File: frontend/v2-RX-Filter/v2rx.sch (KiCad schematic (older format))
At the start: 64 parts, among them P1 CONN_01X09, P4 CONN_01X02, P5 CONN_01X02, U1 4504, U10 PE4259-53, U11 PE4259-53, U12 PE4259-53, U2 PE4259-53, U3 PE4259-53, U4 PE4259-53, U5 PE4259-53, U6 PE4259-53, U7 PE4259-53, U8 PE4259-53, U9 PE4259-53

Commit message: new kicad 4.0.1 stable
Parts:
- C1, C10, C11, C12, C13, C14, C15, C16, C17, C18, C19, C2, C20, C21, C22, C23, C24, C25, C26, C3, C4, C5, C6, C7, C8, C9: symbol C -> C-RESCUE-v2rx
- P1: footprint (none) -> Socket_Strips:Socket_Strip_Straight_1x09
- U1: footprint (none) -> Housings_SOIC:SOIC-16_3.9x9.9mm_Pitch1.27mm
- U10, U11, U12, U2, U3, U4, U5, U6, U7, U8, U9: footprint (none) -> HERMESLITE:sc70-6

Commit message: v2rx changes and update to new kicad
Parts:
- removed C7: 150pF, HERMESLITE:C_0805, symbol C-RESCUE-v2rx
- removed L20: 270nH, HERMESLITE:Choke_SMD_1206_Standard, symbol INDUCTOR
- removed L22: 680nH, HERMESLITE:Choke_SMD_1206_Standard, symbol INDUCTOR
- removed L23: 1.5uH, HERMESLITE:Choke_SMD_1206_Standard, symbol INDUCTOR
- removed P1: CONN_01X09, Socket_Strips:Socket_Strip_Straight_1x09, symbol CONN_01X09
- removed U7: PE4259-53, HERMESLITE:sc70-6, symbol PE4259-53
- added C1, C52, C74, C80, C81: 0.1uF, HERMESLITE:C_0805, symbol C-RESCUE-v2rx
- added C17, C30, C31, C32, C33, C34, C35, C36, C38, C46, C53, C54, C55, C56, C57, C58, C59, C6, C61, C67, C68, C69, C70, C71, C73: DNI, HERMESLITE:C_0805, symbol C-RESCUE-v2rx
- added C26, C48, C64: 330pF, HERMESLITE:C_0805, symbol C-RESCUE-v2rx
- added C27, C49, C65: 560pF, HERMESLITE:C_0805, symbol C-RESCUE-v2rx
- added C29, C43, C51: 1500pF, HERMESLITE:C_0805, symbol C-RESCUE-v2rx
- added C37, C45, C62: 120pF, HERMESLITE:C_0805, symbol C-RESCUE-v2rx
- added C39, C40: 270pF, HERMESLITE:C_0805, symbol C-RESCUE-v2rx
- added C41: 680pF, HERMESLITE:C_0805, symbol C-RESCUE-v2rx
- added C44, C75, C76, C77, C78, C79, C82: 0.01uF, HERMESLITE:C_0805, symbol C-RESCUE-v2rx
- added C47, C63: 180pF, HERMESLITE:C_0805, symbol C-RESCUE-v2rx
- added C50: 1200pF, HERMESLITE:C_0805, symbol C-RESCUE-v2rx
- added C60: 68pF, HERMESLITE:C_0805, symbol C-RESCUE-v2rx
- added C66: 1000pF, HERMESLITE:C_0805, symbol C-RESCUE-v2rx
- added FB1, FB2: BLM21PG220SN1D, symbol FILTER
- added L19: 2.2uH, HERMESLITE:Choke_SMD_1206_Standard, symbol INDUCTOR
- added P1: CONN_02X07, symbol CONN_02X07
- added P3, P4: CONN_02X03, symbol CONN_02X03
- added U10, U11, U2, U3: PE4259-53, HERMESLITE:sc70-6, symbol PE4259-53
- added U9: 4504, Housings_SOIC:SOIC-16_3.9x9.9mm_Pitch1.27mm, symbol 4504
- C10, C11, C12: value 150pF -> DNI
- C13: value 390pF -> DNI
- C14: value 680pF -> DNI
- C15: value 1200pF -> DNI
- C16: value 1000pF -> 68pF
- C18: value 39pF -> 120pF
- C19: value 56pF -> 180pF
- C2: value 100pF -> DNI
- C20: value 150pF -> 330pF
- C21: renamed from C6; value 150pF -> 560pF
- C22: value 150pF -> 1000pF
- C23: value 150pF -> 120pF
- C24, C3: value 270pF -> DNI
- C25: value 560pF -> 180pF
- C28: renamed from C17; value 2200pF -> 1200pF
- C4: value 560pF -> DNI
- C42: renamed from C21; value 150pF -> 1200pF
- C5: value 1000pF -> DNI
- C7: renamed from C1; value 1000pF -> DNI
- C72: renamed from C26; value 1000pF -> DNI
- C8: value 39pF -> DNI
- C9: value 56pF -> DNI
- L1: value 270nH -> 680nH
- L10: value 4.7uH -> 820nH
- L11: value 100nH -> 1.5uH
- L12: value 150nH -> 2.2uH
- L13: value 330nH -> 3.9uH
- L14: value 680nH -> 8.2uH
- L15: value 1.5uH -> 680nH
- L16: value 1uH -> DNI
- L17: value 1.8uH -> 820nH
- L18: value 2.7uH -> 1.5uH
- L2: value 390nH -> DNI
- L20: renamed from L19; value 4.7uH -> 3.9uH
- L21: value 390nH -> 8.2uH
- L3: value 680nH -> 820nH
- L5: value 1.5uH -> 2.2uH
- L6: value 4.7uH -> 3.9uH
- L7: value 1uH -> 8.2uH
- L8: value 1.8uH -> 680nH
- L9: value 2.7uH -> DNI
- renumbered P4 to P2, U8 to U12, U9 to U13, U10 to U14, U11 to U15, U12 to U16, U2 to U4, U3 to U5, U4 to U6, U5 to U7, U6 to U8
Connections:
- net GND: now also C8.2, U12.1 (RF1), U13.1 (RF1), U14.1 (RF1), U15.1 (RF1), U4.1 (RF1), U5.1 (RF1), U6.1 (RF1), U7.1 (RF1), C26.2, C27.2, C29.2, C44.1, C45.2, C46.2, C47.2, C48.2, C49.2, C50.2, C51.2, C52.2, C6.2, C67.2, C68.2, C69.2, C70.2, C71.2, C73.2, C75.1, C76.1, C77.1, C78.1, C79.1, C80.2, C81.1, C82.1, P1.2 (P2), P1.4 (P4), P1.6 (P6), P3.2 (P2), P3.4 (P4), P3.6 (P6), P4.2 (P2), P4.4 (P4), P4.6 (P6), U10.2 (GND), U11.1 (RF1), U11.2 (GND), U2.2 (GND), U3.1 (RF1), U3.2 (GND), U9.8 (VSS); no longer C13.2, C14.2, C15.2, C16.2, L1.2, L11.2, L12.2, L13.2, L14.2, L15.2, L2.2, L21.2, L3.2, L4.2, L5.2, U12.3 (RF2), U13.3 (RF2), U14.3 (RF2), U15.3 (RF2), U4.3 (RF2), U5.3 (RF2), U6.3 (RF2), U7.3 (RF2)
- net at C2.1, L1.1: now also C9.2, U2.5 (RFC); no longer L7.1, U4.5 (RFC)
- net at L7.2: now also C15.1, C22.2; no longer C8.2
- net at C18.2: now also C11.1, L3.2; no longer L16.2
- net at C4.1, L3.1: now also C11.2, U4.5 (RFC); no longer L9.1, U6.5 (RFC)
- net at C10.2: now also C3.1, L2.1, U3.5 (RFC); no longer L9.2
- net at C20.2: now also C13.1, L5.2; no longer L18.2
- net at L8.2: now also C30.1, C37.2; no longer C9.2
- net at C19.2: now also C12.1, L4.2; no longer L17.2
- net at C7.1, L6.1, U7.5 (RFC): now also C14.2; no longer L4.1
- net at C21.1, C28.1: now also L13.1, C35.2; no longer L14.1, L20.1
- net at C21.2, L6.2: now also C14.1
- net at C72.1, U15.5 (RFC): now also C65.1; no longer C22.1, C42.1
- net at U1.14 (Fin): now also P1.1 (P1)
- net at U1.9 (Din): now also P1.5 (P5)
- net at U1.11 (Ein): now also P1.7 (P7)
- net at U1.7 (Cin): now also P1.9 (P9)
- net at U1.5 (Bin): now also P1.11 (P11)
- net at U1.3 (Ain): now also P1.12 (P12)
- net at U1.15 (Fout): now also U10.4 (CTRL), U2.4 (CTRL)
- net 3.3V: no longer names the net of U1.16 (VDD), U12.6 (/CTRL), U13.6 (/CTRL), U14.6 (/CTRL), U15.6 (/CTRL), U16.6 (/CTRL), U4.6 (/CTRL), U5.6 (/CTRL), U6.6 (/CTRL), U7.6 (/CTRL), U8.6 (/CTRL)
- net 3.3V: now also C81.2, FB2.2, U10.6 (/CTRL), U11.6 (/CTRL), U2.6 (/CTRL), U3.6 (/CTRL), U9.16 (VDD)
- net 5V: no longer names the net of U1.1 (VCC), U1.13 (Select)
- net 5V: now also C52.1, C80.1, FB1.2, U9.1 (VCC), U9.13 (Select)
- new net: C74.1, P5.2 (P2)
- new net: C1.2, P2.2 (P2)
- new net: C42.1, C50.1, C58.2, L20.1
- new net: C35.1, C42.2, L13.2
- new net: C58.1, C65.2, L20.2
- new net: C1.1, P3.3 (P3), U3.3 (RF2), U4.3 (RF2), U5.3 (RF2), U6.3 (RF2), U7.3 (RF2), U8.3 (RF2)
- new net: C15.2, C8.1, L7.1, U8.5 (RFC)
- new net: C74.2, P4.3 (P3), U11.3 (RF2), U12.3 (RF2), U13.3 (RF2), U14.3 (RF2), U15.3 (RF2), U16.3 (RF2)
- new net: C66.1, C73.1, U16.5 (RFC)
- new net: C13.2, C6.1, L5.1, U6.5 (RFC)
- new net: C12.2, C5.1, L4.1, U5.5 (RFC)
- new net: C64.1, C71.1, U14.5 (RFC)
- new net: C63.1, C70.1, U13.5 (RFC)
- new net: C62.1, C69.1, U12.5 (RFC)
- new net: FB1.1, P1.10 (P10)
- new net: FB2.1, P1.13 (P13)
- new net: P1.3 (P3), U9.3 (Ain)
- new net: C22.1, C29.1, C36.2, L14.1
- new net: C43.1, C51.1, C59.2, L21.1
- new net: C36.1, C43.2, L14.2
- new net: C59.1, C66.2, L21.2
- new net: C20.1, C27.1, C34.2, L12.1
- new net: C41.1, C49.1, C57.2, L19.1
- new net: C34.1, C41.2, L12.2
- new net: C57.1, C64.2, L19.2
- new net: C19.1, C26.1, C33.2, L11.1
- new net: C40.1, C48.1, C56.2, L18.1
- new net: C33.1, C40.2, L11.2
- new net: C56.1, C63.2, L18.2
- new net: C18.1, C25.1, C32.2, L10.1
- new net: C39.1, C47.1, C55.2, L17.1
- new net: C32.1, C39.2, L10.2
- new net: C55.1, C62.2, L17.2
- new net: U11.4 (CTRL), U3.4 (CTRL), U9.2 (Aout)
- new net: C61.1, C68.1, U11.5 (RFC)
- new net: C17.1, C24.1, C31.2, L9.1
- new net: C10.1, C17.2, L2.2
- new net: C38.1, C46.1, C54.2, L16.1
- new net: C31.1, C38.2, L9.2
- new net: C54.1, C61.2, L16.2
- new net: P3.1 (P1), U2.1 (RF1)
- new net: P3.5 (P5), U2.3 (RF2)
- new net: P4.1 (P1), U10.1 (RF1)
- new net: P4.5 (P5), U10.3 (RF2)
- new net: C60.1, C67.1, U10.5 (RFC)
- new net: C16.1, C23.1, C30.2, L8.1
- new net: C16.2, C9.1, L1.2
- new net: C37.1, C45.1, C53.2, L15.1
- new net: C53.1, C60.2, L15.2
- no-connect marks 2 -> 13
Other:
- note added: "(DNI)"
- note added: "10/12M\n"
- note added: "160M\n"
- note added: "17/15M\n"
- note added: "30/20M\n"
- note added: "3v3 from\nV2 frontend"
- note added: "60/40M\n"
- note added: "80/75M\n"
- note added: "Common brings in\n 12V from PA"
- note added: "From pre-V2 TX design\nBand0 - 160M\nBand1 - 80/75M\nBand2 - 60/40M\nBand3 - 30/20M\nBand4 - 17/15M\nBand5 - spare\nBand6 - 10/12M inverted"
- note added: "Jumper Pins 3 to 5 if normal logic\nJumper pins 1 - 3 if inverted logic\nGround unused pin to 2, 4 or 6 as needed"
- note added: "Spare\n"
- note removed: "14-20MHz values,\nneeds 30M/20M BPF"
- note removed: "160M"
- note removed: "20-30MHz values,\nneeds to be 17m/15m BPF"
- note removed: "3-5MHz\nMay want to tighten this up to 4mhz"
- note removed: "7-10MHz values,\nneeds to be 60M/40M BPF"
- note removed: "Band0\nBand1\nBand2\nBand3\nBand4\nBand5\nBand6\nextra\nGnd"
- note removed: "Bypass"
- note removed: "From pre-V2 TX design\nBand0 - 160M\nBand1 - 80/75M\nBand2 - 60/40M\nBand3 - 30/20M\nBand4 - 17/15M\nBand5 - unused\nBand6 - 10/12M inverted"
- note removed: "Notes - Need to determine how to obtain\n3.3V and 5V - 12v with regulators on board or\njumper from v2 main board to supply voltages."
- moved on the sheet: C21, C28, C42, C7, C72, L20, L6, P2, P5, U1, U12, U13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

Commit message: Latest Rx updates
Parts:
- FB1, FB2: footprint (none) -> Resistors_SMD:R_0805_HandSoldering
- L1, L10, L11, L12, L13, L14, L15, L16, L17, L18, L19, L2, L20, L21, L3, L4, L5, L6, L7, L8, L9: footprint HERMESLITE:Choke_SMD_1206_Standard -> HERMESLITE:inductor
- P1: footprint (none) -> Pin_Headers:Pin_Header_Straight_2x07
- P3, P4: footprint (none) -> Pin_Headers:Pin_Header_Straight_2x03
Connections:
- net at U1.2 (Aout), U16.4 (CTRL), U8.4 (CTRL): now also C82.2
- net at U1.4 (Bout), U15.4 (CTRL), U7.4 (CTRL): now also C79.2
- net at U1.6 (Cout), U14.4 (CTRL), U6.4 (CTRL): now also C78.2
- net at U1.10 (Dout), U13.4 (CTRL), U5.4 (CTRL): now also C77.2
- net at U1.12 (Eout), U12.4 (CTRL), U4.4 (CTRL): now also C76.2
- net at U1.15 (Fout), U10.4 (CTRL), U2.4 (CTRL): now also C44.2
- net at U11.4 (CTRL), U3.4 (CTRL), U9.2 (Aout): now also C75.2

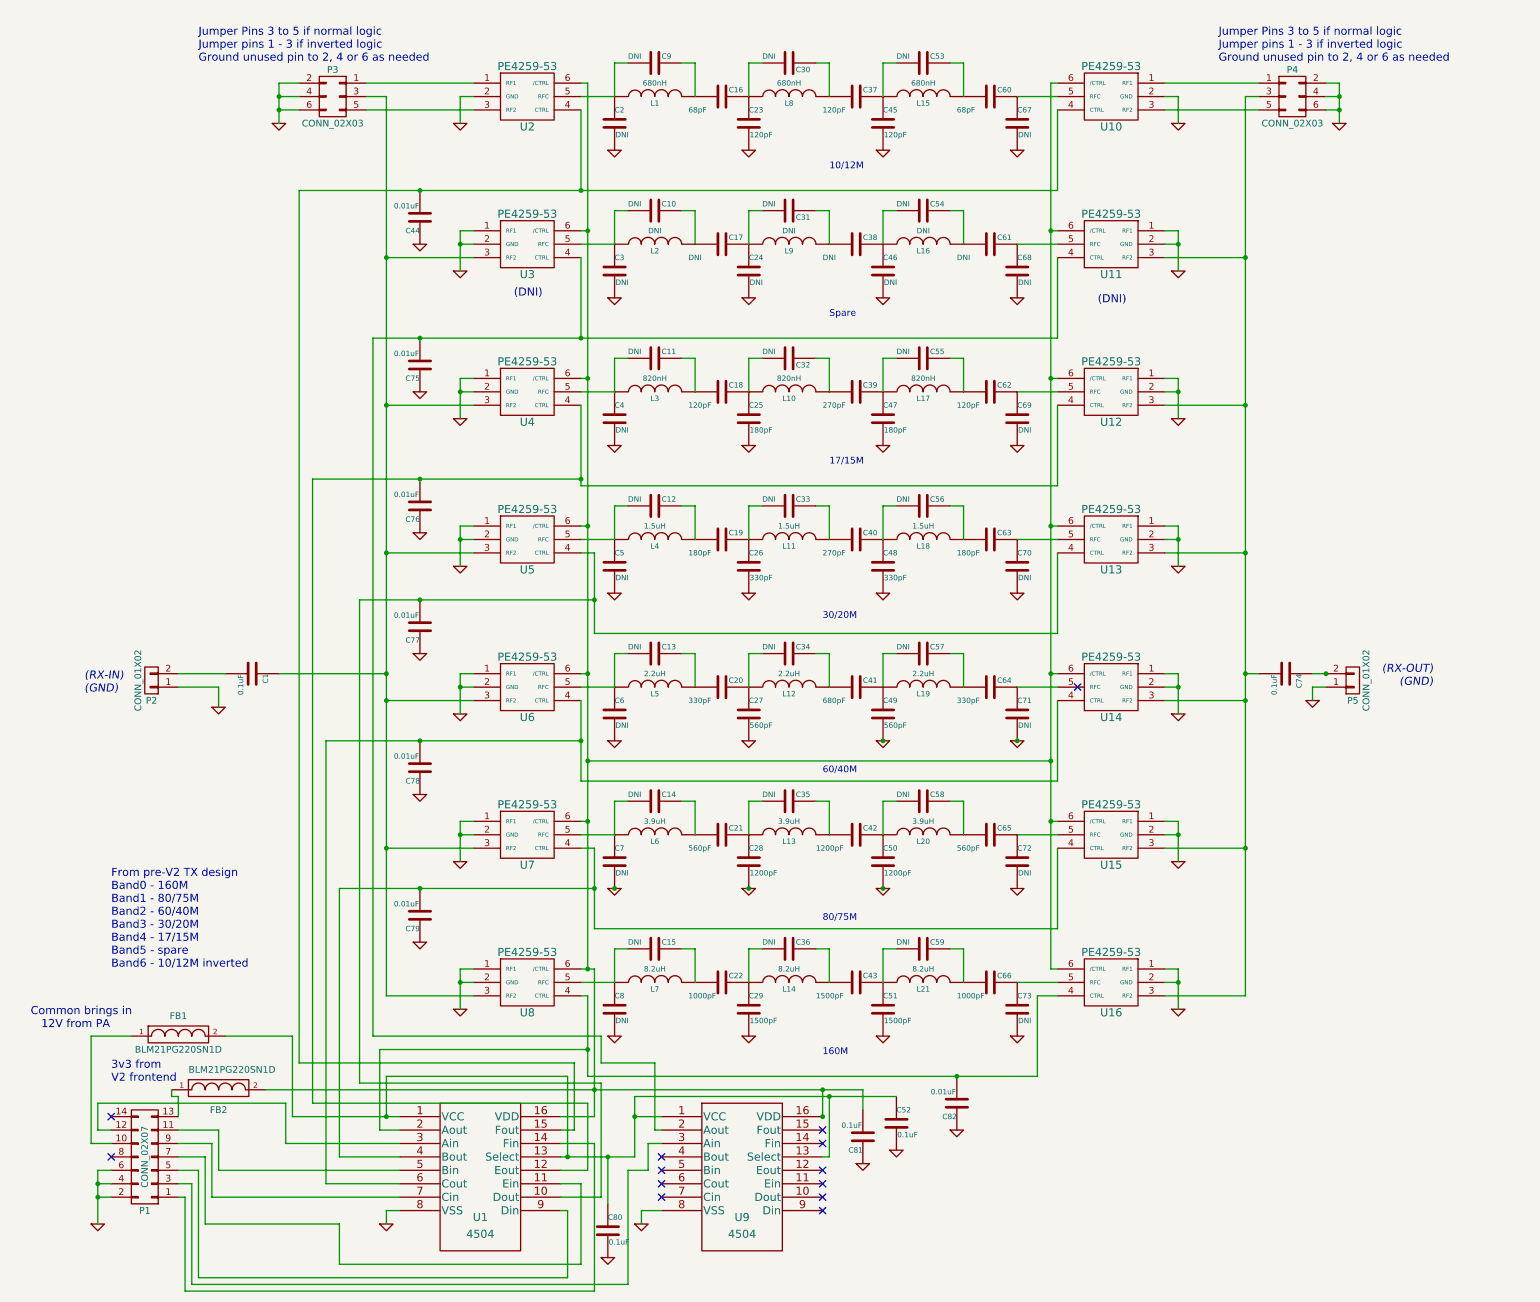
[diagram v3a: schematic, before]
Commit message: New RX Filter Board Layout
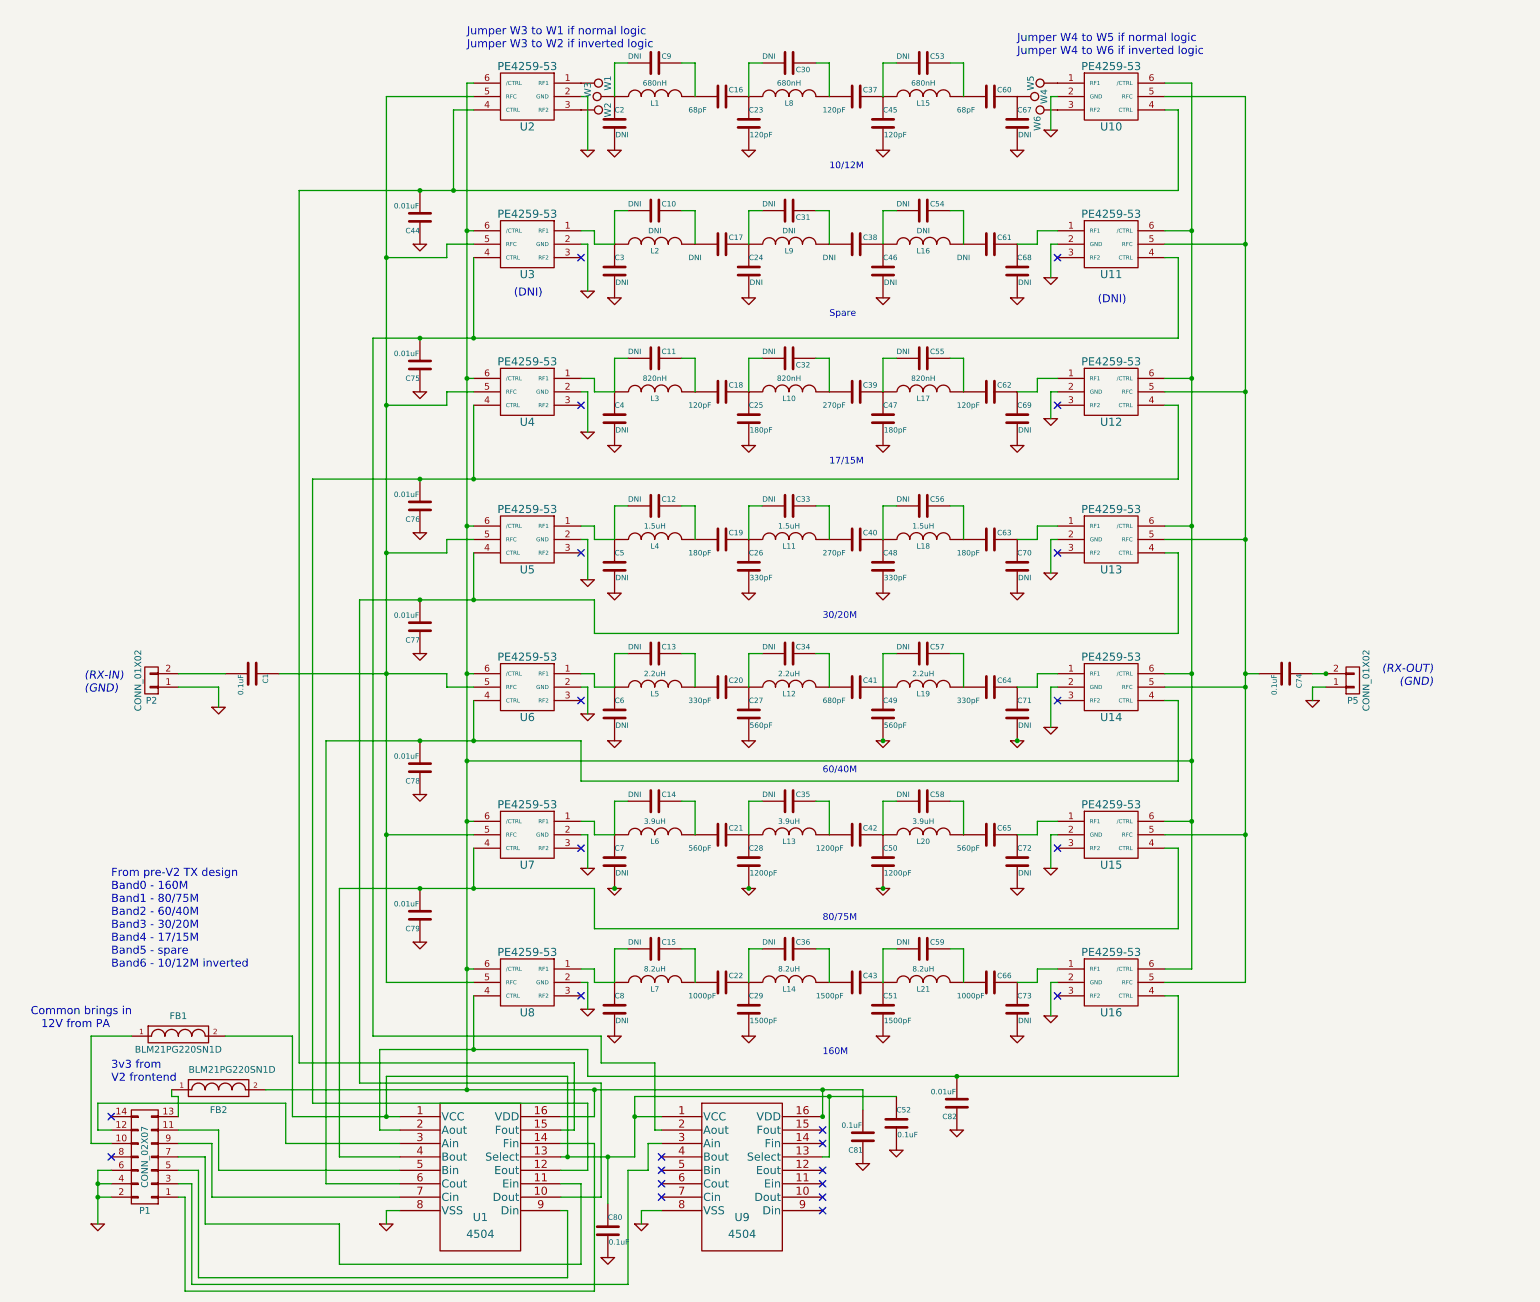
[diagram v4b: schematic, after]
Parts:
- removed P3, P4: CONN_02X03, Pin_Headers:Pin_Header_Straight_2x03, symbol CONN_02X03
- added W1, W2, W3, W4, W5, W6: TEST_1P, Wire_Pads:SolderWirePad_single_0-8mmDrill, symbol TEST_1P
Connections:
- net GND: no longer U11.1 (RF1), U12.1 (RF1), U13.1 (RF1), U14.1 (RF1), U15.1 (RF1), U16.1 (RF1), U3.1 (RF1), U4.1 (RF1), U5.1 (RF1), U6.1 (RF1), U7.1 (RF1), U8.1 (RF1)
- net at C14.2, C7.1, L6.1: now also U7.1 (RF1); no longer U7.5 (RFC)
- net at C65.1, C72.1: now also U15.1 (RF1); no longer U15.5 (RFC)
- net at C15.2, C8.1, L7.1: now also U8.1 (RF1); no longer U8.5 (RFC)
- net at C66.1, C73.1: now also U16.1 (RF1); no longer U16.5 (RFC)
- net at C13.2, C6.1, L5.1: now also U6.1 (RF1); no longer U6.5 (RFC)
- net at C12.2, C5.1, L4.1: now also U5.1 (RF1); no longer U5.5 (RFC)
- net at C11.2, C4.1, L3.1: now also U4.1 (RF1); no longer U4.5 (RFC)
- net at C64.1, C71.1: now also U14.1 (RF1); no longer U14.5 (RFC)
- net at C63.1, C70.1: now also U13.1 (RF1); no longer U13.5 (RFC)
- net at C62.1, C69.1: now also U12.1 (RF1); no longer U12.5 (RFC)
- net at C10.2, C3.1, L2.1: now also U3.1 (RF1); no longer U3.5 (RFC)
- net at C61.1, C68.1: now also U11.1 (RF1); no longer U11.5 (RFC)
- net at U2.1 (RF1): now also W1.1
- net at U2.3 (RF2): now also W2.1
- net at C2.1, C9.2, L1.1: now also W3.1; no longer U2.5 (RFC)
- net at U10.1 (RF1): now also W5.1
- net at U10.3 (RF2): now also W6.1
- net at C60.1, C67.1: now also W4.1; no longer U10.5 (RFC)
- new net: C1.1, U2.5 (RFC), U3.5 (RFC), U4.5 (RFC), U5.5 (RFC), U6.5 (RFC), U7.5 (RFC), U8.5 (RFC)
- new net: C74.2, U10.5 (RFC), U11.5 (RFC), U12.5 (RFC), U13.5 (RFC), U14.5 (RFC), U15.5 (RFC), U16.5 (RFC)
- now unconnected: U11.3 (RF2), U12.3 (RF2), U13.3 (RF2), U14.3 (RF2), U15.3 (RF2), U16.3 (RF2), U3.3 (RF2), U4.3 (RF2), U5.3 (RF2), U6.3 (RF2), U7.3 (RF2), U8.3 (RF2)
- no-connect marks 13 -> 24
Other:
- note added: "Jumper W3 to W1 if normal logic\nJumper W3 to W2 if inverted logic"
- note added: "Jumper W4 to W5 if normal logic\nJumper W4 to W6 if inverted logic"
- note removed: "Jumper Pins 3 to 5 if normal logic\nJumper pins 1 - 3 if inverted logic\nGround unused pin to 2, 4 or 6 as needed"
